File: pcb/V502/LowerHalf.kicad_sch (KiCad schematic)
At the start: 12 parts, among them J1 Conn_01x30_Pin, J2 Conn_01x30_Pin, J3 Conn_01x30_Pin, J4 Conn_01x30_Pin, U13 74LS574, U14 74LS574, U15 74LS245, U16 74LS245

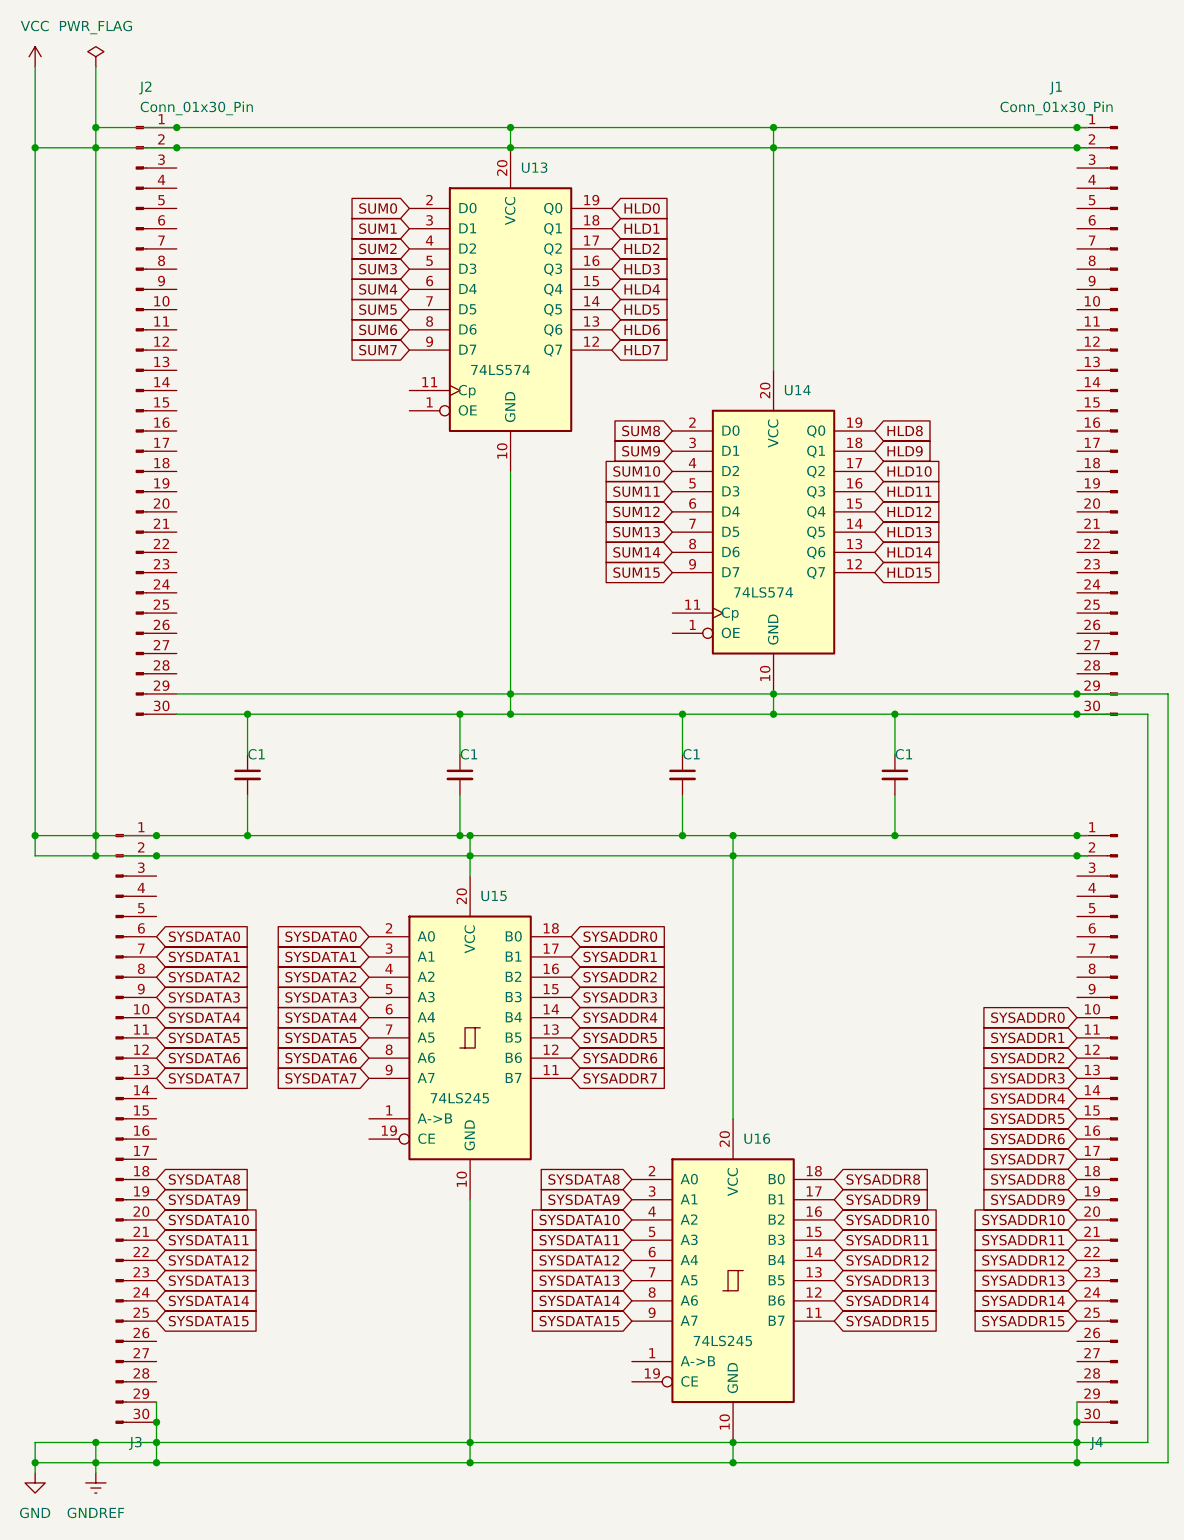
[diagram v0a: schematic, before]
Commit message: V502 board almost completely routed.
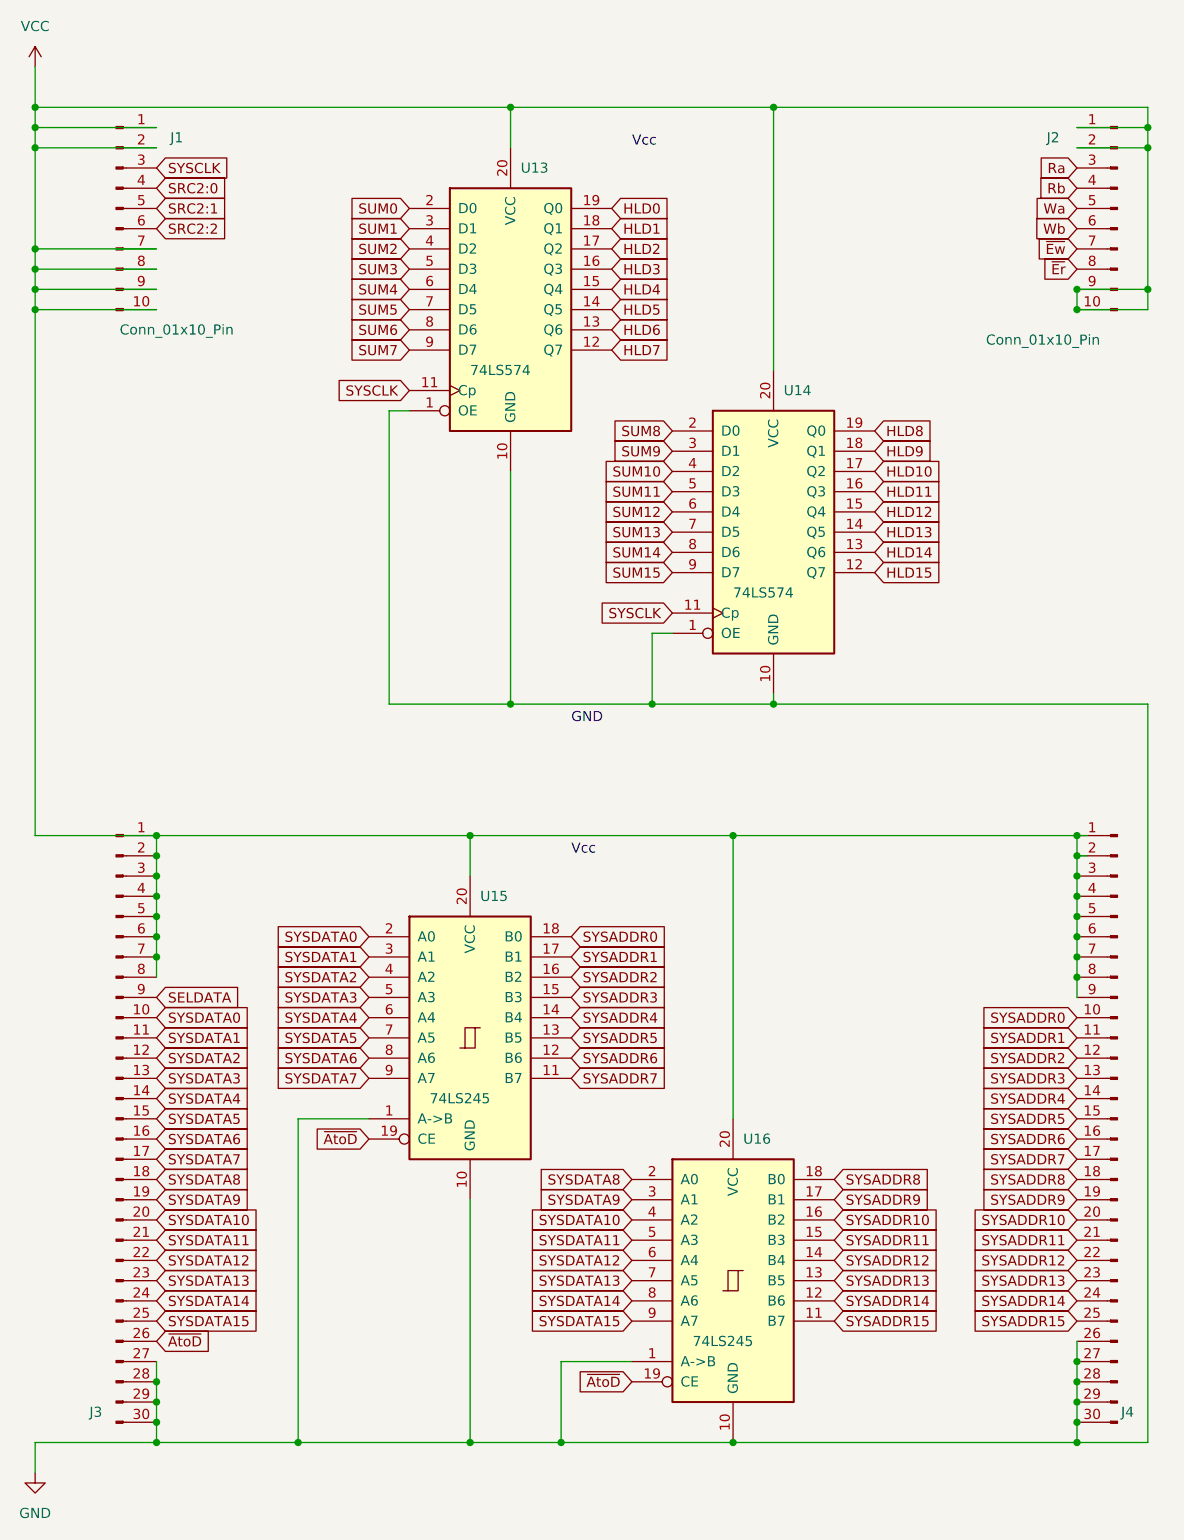
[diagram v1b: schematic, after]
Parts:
- removed C1 (x4): C_Small, Capacitor_THT:C_Disc_D3.0mm_W2.0mm_P2.50mm, symbol Device:C_Small
- removed J1, J2: Conn_01x30_Pin, Connector_PinHeader_2.54mm:PinHeader_1x30_P2.54mm_Vertical, symbol Connector:Conn_01x30_Pin
- added J1, J2: Conn_01x10_Pin, Connector_PinHeader_2.54mm:PinHeader_1x10_P2.54mm_Vertical, symbol Connector:Conn_01x10_Pin
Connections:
- net GND: now also J3.27 (Pin_27), J3.28 (Pin_28), J4.26 (Pin_26), J4.27 (Pin_27), J4.28 (Pin_28), U13.1 (OE), U14.1 (OE), U15.1 (A->B), U16.1 (A->B)
- net SYSDATA0: now also J3.10 (Pin_10); no longer J3.6 (Pin_6)
- net SYSDATA1: now also J3.11 (Pin_11); no longer J3.7 (Pin_7)
- net SYSDATA2: now also J3.12 (Pin_12); no longer J3.8 (Pin_8)
- net SYSDATA3: now also J3.13 (Pin_13); no longer J3.9 (Pin_9)
- net SYSDATA4: now also J3.14 (Pin_14); no longer J3.10 (Pin_10)
- net SYSDATA5: now also J3.15 (Pin_15); no longer J3.11 (Pin_11)
- net SYSDATA6: now also J3.16 (Pin_16); no longer J3.12 (Pin_12)
- net SYSDATA7: now also J3.17 (Pin_17); no longer J3.13 (Pin_13)
- net VCC: now also J3.3 (Pin_3), J3.4 (Pin_4), J3.5 (Pin_5), J3.6 (Pin_6), J3.7 (Pin_7), J3.8 (Pin_8), J4.3 (Pin_3), J4.4 (Pin_4), J4.5 (Pin_5), J4.6 (Pin_6), J4.7 (Pin_7), J4.8 (Pin_8), J4.9 (Pin_9), J1.1 (Pin_1), J1.10 (Pin_10), J1.2 (Pin_2), J1.7 (Pin_7), J1.8 (Pin_8), J1.9 (Pin_9), J2.1 (Pin_1), J2.10 (Pin_10), J2.2 (Pin_2), J2.9 (Pin_9)
- net ~{AtoD}: now reaches J3.26 (Pin_26)
- net ~{AtoD}: now also U15.19 (CE), U16.19 (CE)
- net SYSCLK: now reaches U14.11 (Cp)
- net SYSCLK: now also U13.11 (Cp), J1.3 (Pin_3)
- new net Ra: J2.3 (Pin_3)
- new net Rb: J2.4 (Pin_4)
- new net SELDATA: J3.9 (Pin_9)
- new net SRC2:0: J1.4 (Pin_4)
- new net SRC2:1: J1.5 (Pin_5)
- new net SRC2:2: J1.6 (Pin_6)
- new net Wa: J2.5 (Pin_5)
- new net Wb: J2.6 (Pin_6)
- new net ~{Er}: J2.8 (Pin_8)
- new net ~{Ew}: J2.7 (Pin_7)
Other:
- note added: "GND"
- note added: "Vcc"

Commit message: V502 is complete. Freezing it permanently.
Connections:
- net GND: now also J2.1 (Pin_1), J2.10 (Pin_10), J2.2 (Pin_2), J2.9 (Pin_9), J4.1 (Pin_1), J4.2 (Pin_2), J4.3 (Pin_3), J4.4 (Pin_4), J4.5 (Pin_5), J4.6 (Pin_6), J4.7 (Pin_7), J4.8 (Pin_8), J4.9 (Pin_9); no longer J3.27 (Pin_27), J3.28 (Pin_28), J3.29 (Pin_29), J3.30 (Pin_30)
- net VCC: now also J3.27 (Pin_27), J3.28 (Pin_28), J3.29 (Pin_29), J3.30 (Pin_30); no longer J2.1 (Pin_1), J2.10 (Pin_10), J2.2 (Pin_2), J2.9 (Pin_9), J4.1 (Pin_1), J4.2 (Pin_2), J4.3 (Pin_3), J4.4 (Pin_4), J4.5 (Pin_5), J4.6 (Pin_6), J4.7 (Pin_7), J4.8 (Pin_8), J4.9 (Pin_9)
